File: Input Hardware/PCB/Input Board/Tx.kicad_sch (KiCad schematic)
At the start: 32 parts

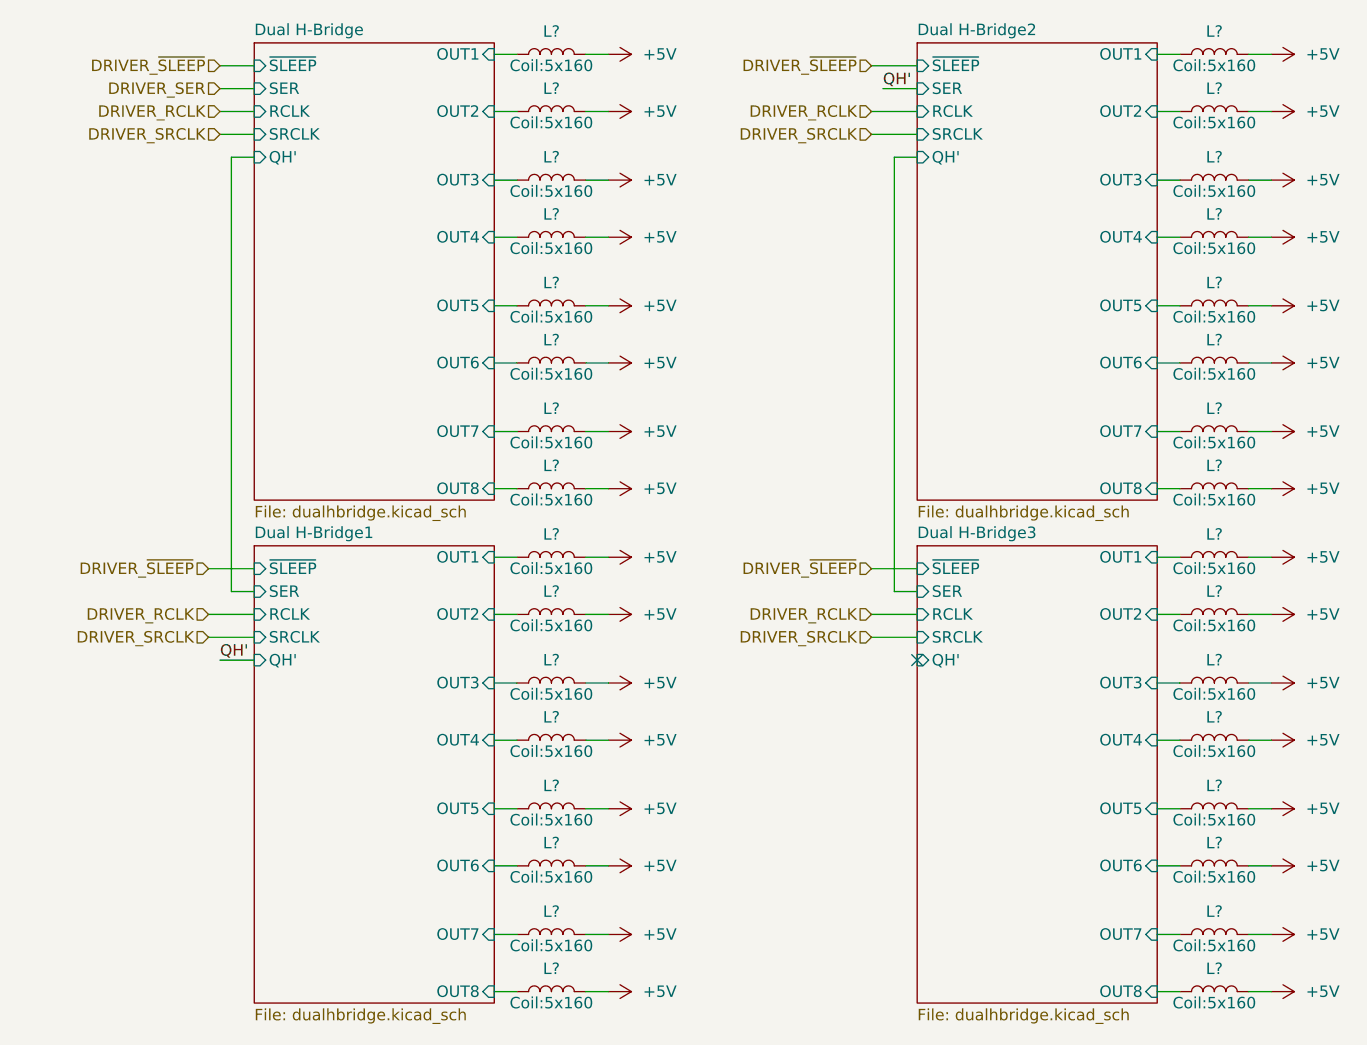
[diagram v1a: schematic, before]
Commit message: package type change
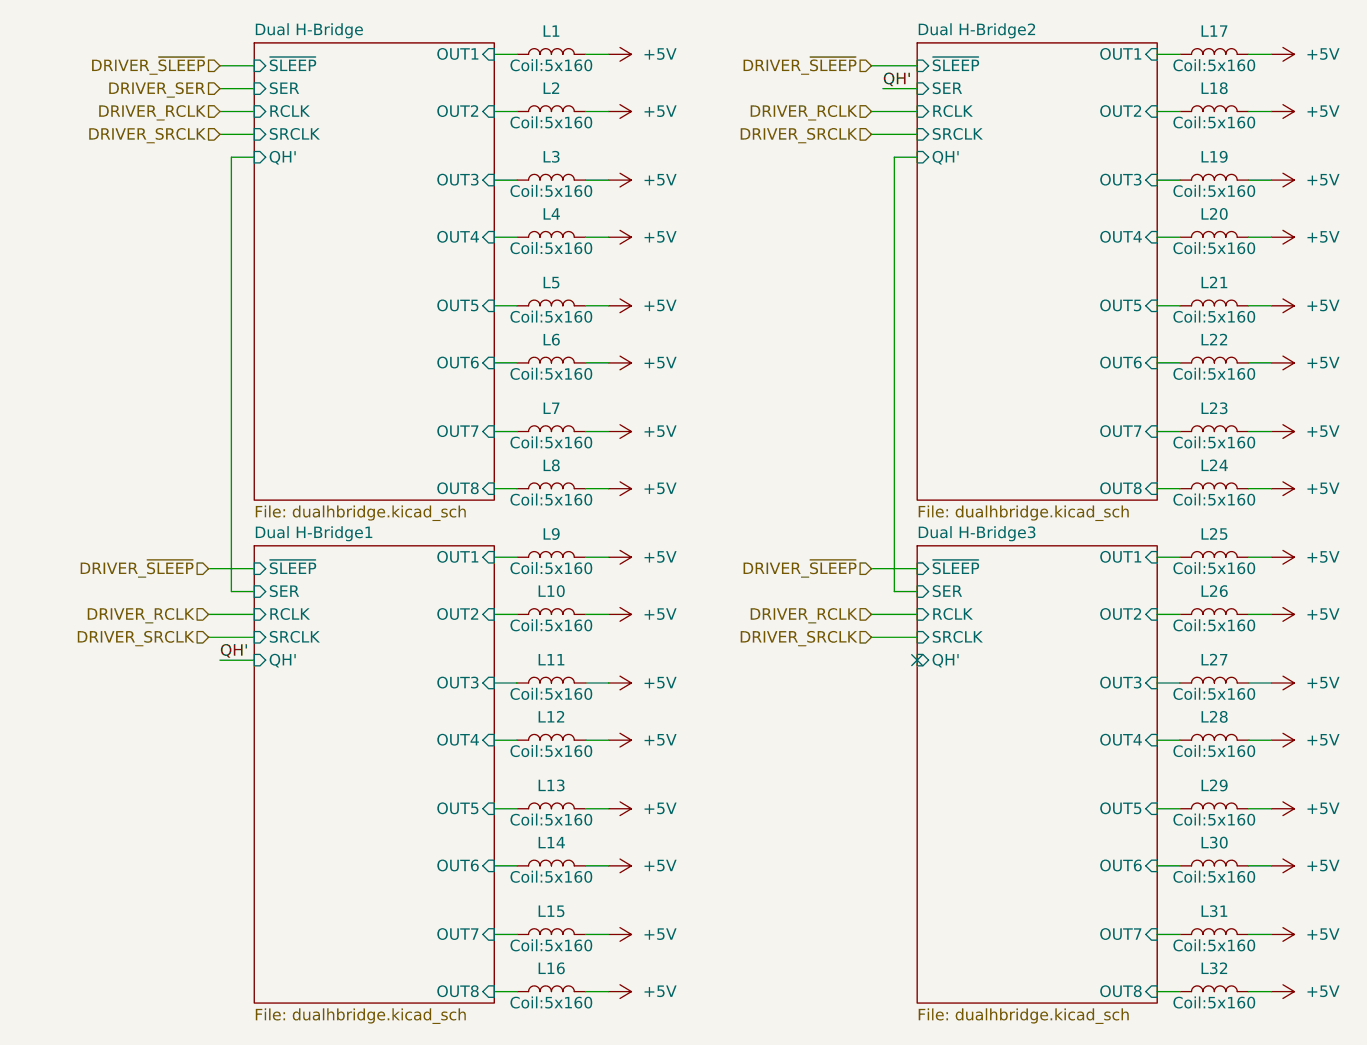
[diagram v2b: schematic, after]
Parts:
- gave numbers to parts that had none: 32

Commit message: Schematic Cleanup
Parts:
- renumbered L19 to L?, L24 to L?, L6 to L?, L3 to L?, L8 to L?, L27 to L?, L7 to L?, L30 to L?, L26 to L?, L4 to L?, L13 to L?, L14 to L?, L11 to L?, L17 to L?, L10 to L?, L31 to L?, L2 to L?, L1 to L?, L5 to L?, L20 to L?, L15 to L?, L23 to L?, L16 to L?, L22 to L?, L18 to L?, L29 to L?, L25 to L?, L28 to L?, L12 to L?, L32 to L?, L9 to L?, L21 to L?
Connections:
- net +5V renamed GND
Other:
- sheet Dual H-Bridge renamed Dual H-Bridge 1
- sheet Dual H-Bridge1 renamed Dual H-Bridge 2
- sheet Dual H-Bridge2 renamed Dual H-Bridge 3
- sheet Dual H-Bridge3 renamed Dual H-Bridge 4
- sheet Dual H-Bridge 1 ports: added none; removed ~{SLEEP}
- sheet Dual H-Bridge 2 ports: added none; removed ~{SLEEP}
- sheet Dual H-Bridge 3 ports: added none; removed ~{SLEEP}
- sheet Dual H-Bridge 4 ports: added none; removed ~{SLEEP}
- moved on the sheet: L?

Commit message: Layout Progress
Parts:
- gave numbers to parts that had none: 32

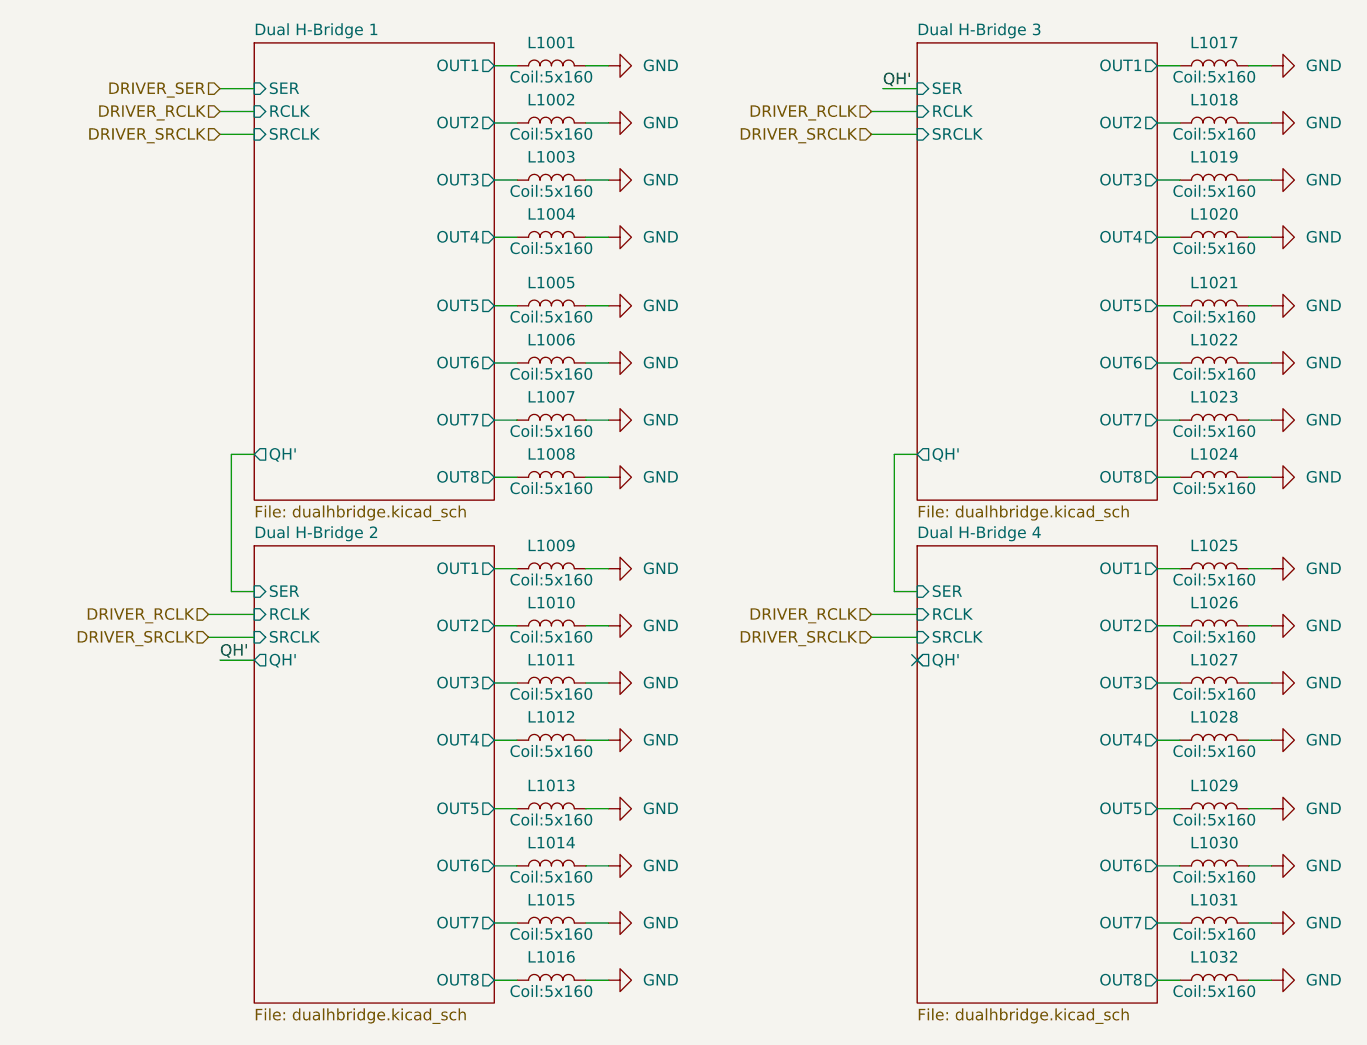
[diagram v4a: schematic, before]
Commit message: sleep pin rewire
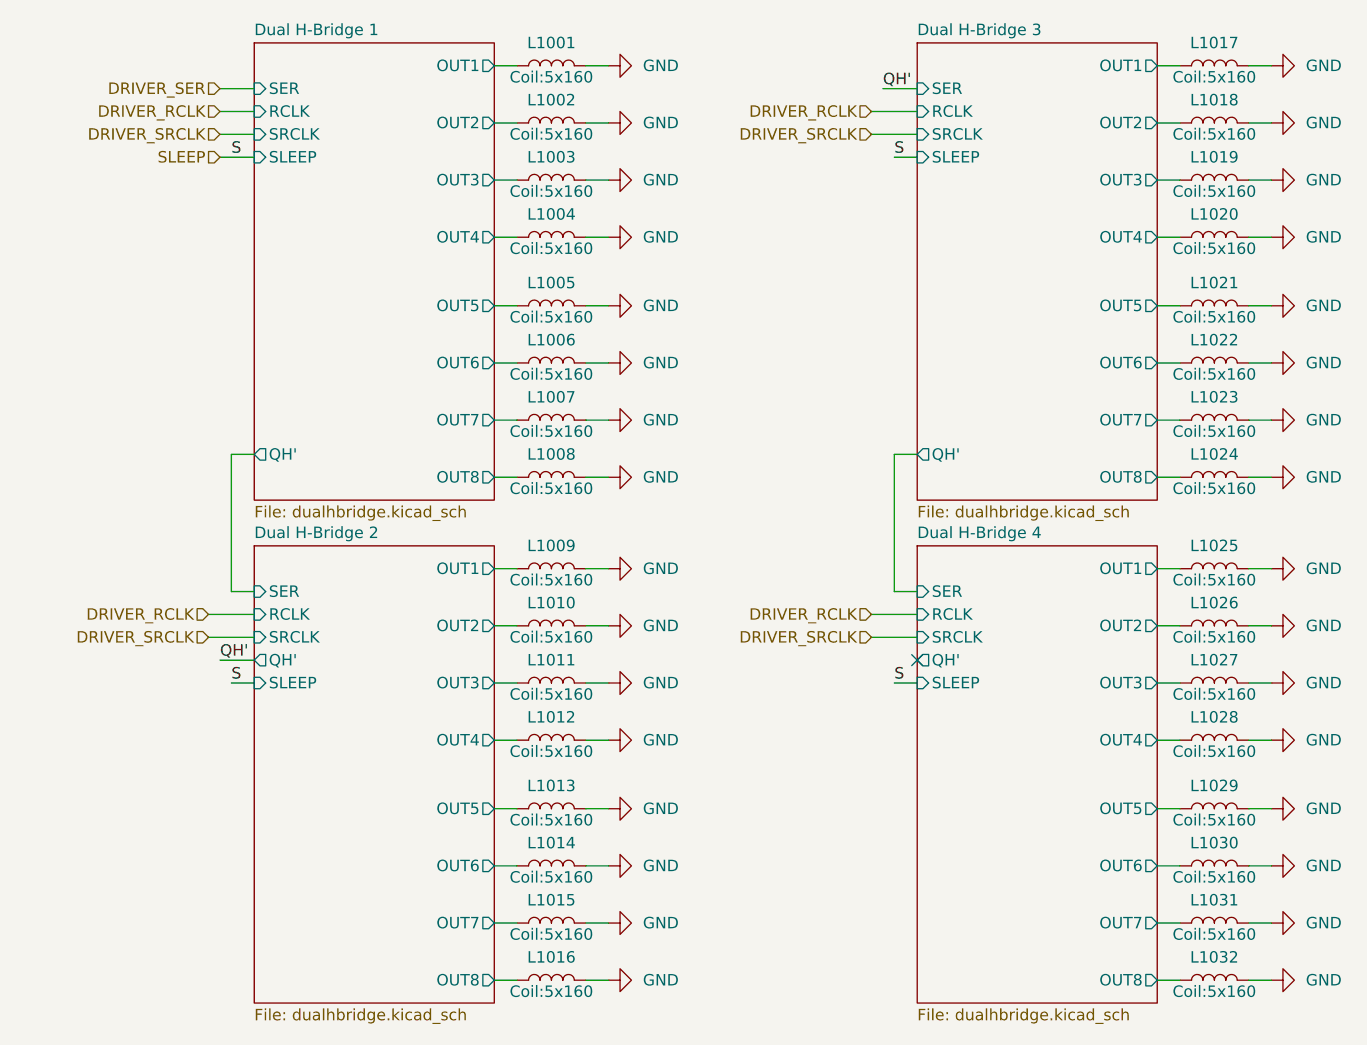
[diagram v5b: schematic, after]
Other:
- sheet Dual H-Bridge 1 ports: added SLEEP; removed none
- sheet Dual H-Bridge 2 ports: added SLEEP; removed none
- sheet Dual H-Bridge 3 ports: added SLEEP; removed none
- sheet Dual H-Bridge 4 ports: added SLEEP; removed none
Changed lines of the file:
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@@
 	(wire
 		(pts
+			(xy 97.79 36.83) (xy 101.6 36.83)
+		)
+		(stroke
+			(width 0)
+			(type default)
+		)
+	)
+	(wire
+		(pts
 			(xy 138.43 33.02) (xy 140.97 33.02)
 		)
@@
 	(wire
 		(pts
+			(xy 172.72 36.83) (xy 175.26 36.83)
+		)
+		(stroke
+			(width 0)
+			(type default)
+		)
+	)
+	(wire
+		(pts
 			(xy 128.27 95.25) (xy 130.81 95.25)
 		)
@@
 	(wire
 		(pts
+			(xy 172.72 95.25) (xy 175.26 95.25)
+		)
+		(stroke
+			(width 0)
+			(type default)
+		)
+	)
+	(wire
+		(pts
 			(xy 212.09 45.72) (xy 214.63 45.72)
 		)
@@
 	(wire
 		(pts
+			(xy 99.06 95.25) (xy 101.6 95.25)
+		)
+		(stroke
+			(width 0)
+			(type default)
+		)
+	)
+	(wire
+		(pts
 			(xy 138.43 115.57) (xy 140.97 115.57)
 		)
@@
 		)
 	)
+	(label "S "
+		(at 99.06 36.83 0)
+		(effects
+			(font
+				(size 1.27 1.27)
+			)
+			(justify left bottom)
+		)
+	)
+	(label "S "
+		(at 172.72 36.83 0)
+		(effects
+			(font
+				(size 1.27 1.27)
+			)
+			(justify left bottom)
+		)
+	)
+	(label "S "
+		(at 99.06 95.25 0)
+		(effects
+			(font
+				(size 1.27 1.27)
+			)
+			(justify left bottom)
+		)
+	)
+	(label "S "
+		(at 172.72 95.25 0)
+		(effects
+			(font
+				(size 1.27 1.27)
+			)
+			(justify left bottom)
+		)
+	)
 	(hierarchical_label "DRIVER_SRCLK"
 		(shape input)
@@
 		)
 	)
+	(hierarchical_label "SLEEP"
+		(shape input)
+		(at 97.79 36.83 180)
+		(effects
+			(font
+				(size 1.27 1.27)
+			)
+			(justify right)
+		)
+	)
 	(hierarchical_label "DRIVER_SRCLK"
 		(shape input)
@@
 			)
 		)
+		(pin "SLEEP" input
+			(at 101.6 36.83 180)
+			(effects
+				(font
+					(size 1.27 1.27)
+				)
+				(justify left)
+			)
+		)
 		(instances
 			(project "Input Board"
@@
 			)
 		)
+		(pin "SLEEP" input
+			(at 175.26 36.83 180)
+			(effects
+				(font
+					(size 1.27 1.27)
+				)
+				(justify left)
+			)
+		)
 		(instances
 			(project "Input Board"
@@
 			)
 		)
+		(pin "SLEEP" input
+			(at 101.6 95.25 180)
+			(effects
+				(font
+					(size 1.27 1.27)
+				)
+				(justify left)
+			)
+		)
 		(instances
 			(project "Input Board"
@@
 			)
 		)
+		(pin "SLEEP" input
+			(at 175.26 95.25 180)
+			(effects
+				(font
+					(size 1.27 1.27)
+				)
+				(justify left)
+			)
+		)
